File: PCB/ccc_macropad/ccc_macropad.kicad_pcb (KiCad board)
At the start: 2 copper layers, 101.5 x 44 mm, 18 parts, among them SW1 SW_Push, SW2 SW_Push, SW3 OS/Left_Right-hand_Switch, SW4 SW_Push, SW5 SW_Push, U1 RP2040-Zero

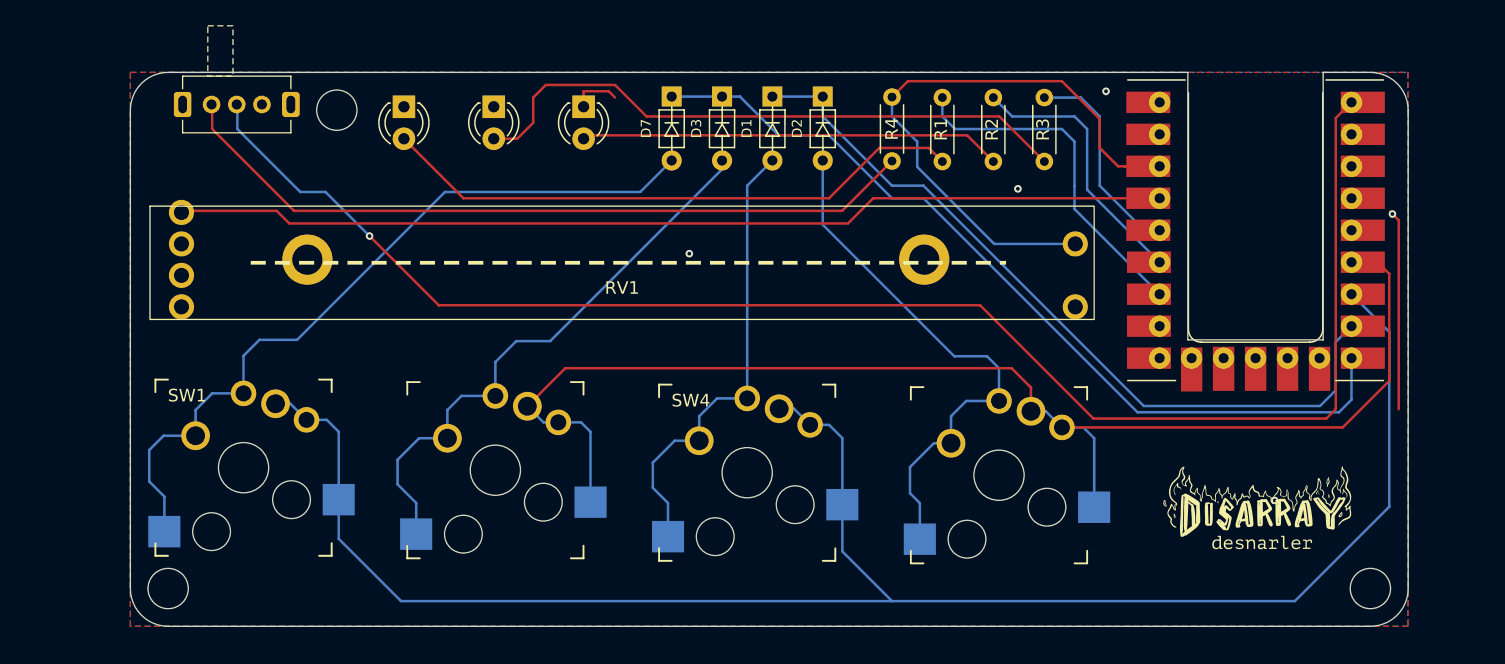
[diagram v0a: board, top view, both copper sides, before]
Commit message: feat: add buffer capacitor//increase board size// add foot holes
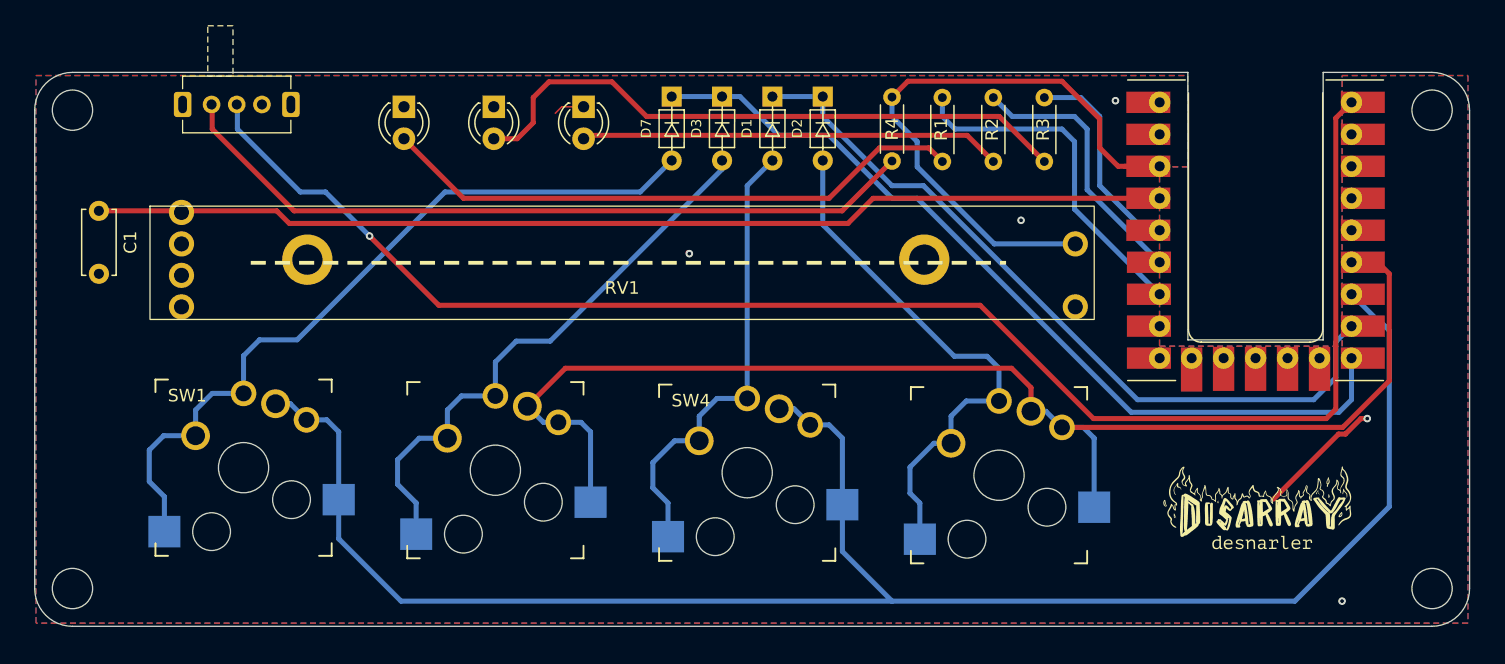
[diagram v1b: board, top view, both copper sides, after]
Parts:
- added C1: C, Capacitor_THT:C_Disc_D5.0mm_W2.5mm_P5.00mm, F.Cu at (108.0, 49.0)
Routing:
- net GND: track 20.4 -> 12.7 mm
- net Net-(U1-GP29): track 78.1 -> 84.7 mm
- net Net-(D1-K): track 62.0 -> 61.0 mm
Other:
- board size 101.5 x 44 mm -> 114 x 44 mm

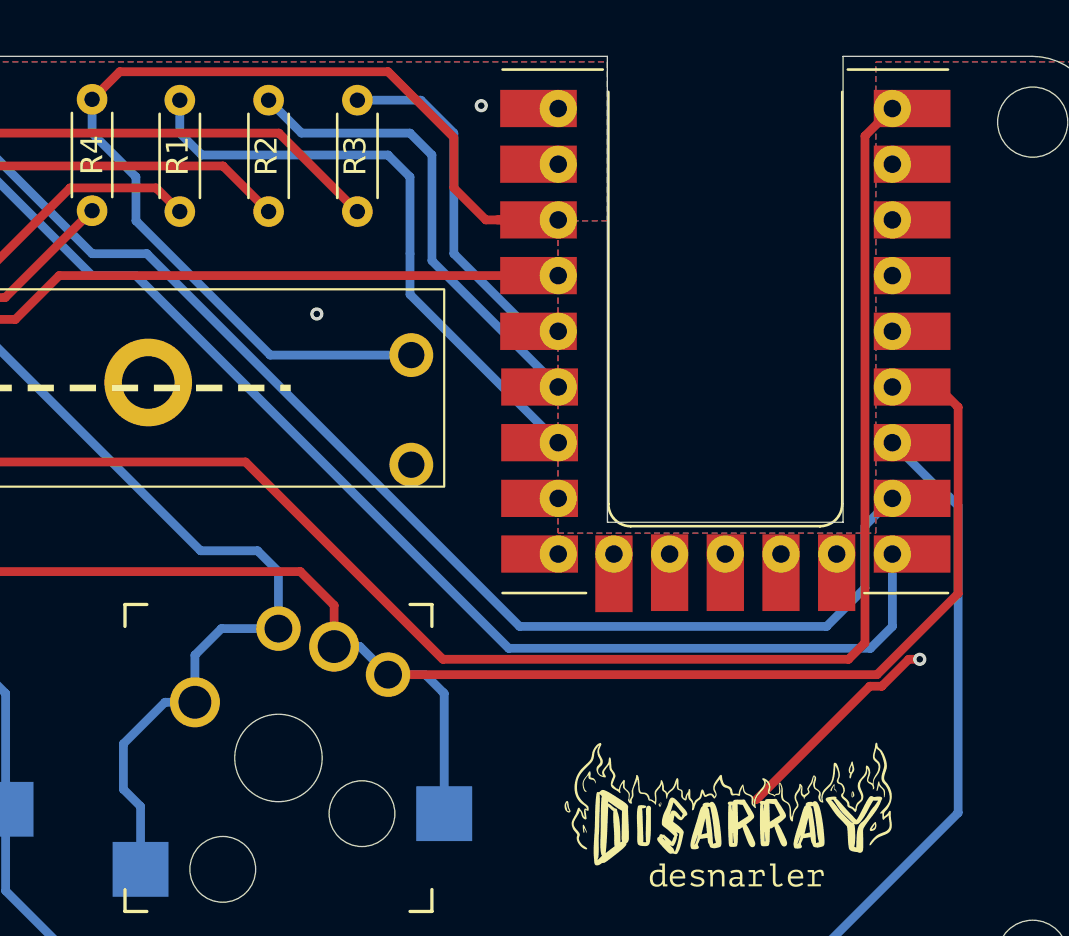
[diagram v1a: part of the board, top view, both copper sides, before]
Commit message: refactoring: mini adjustments
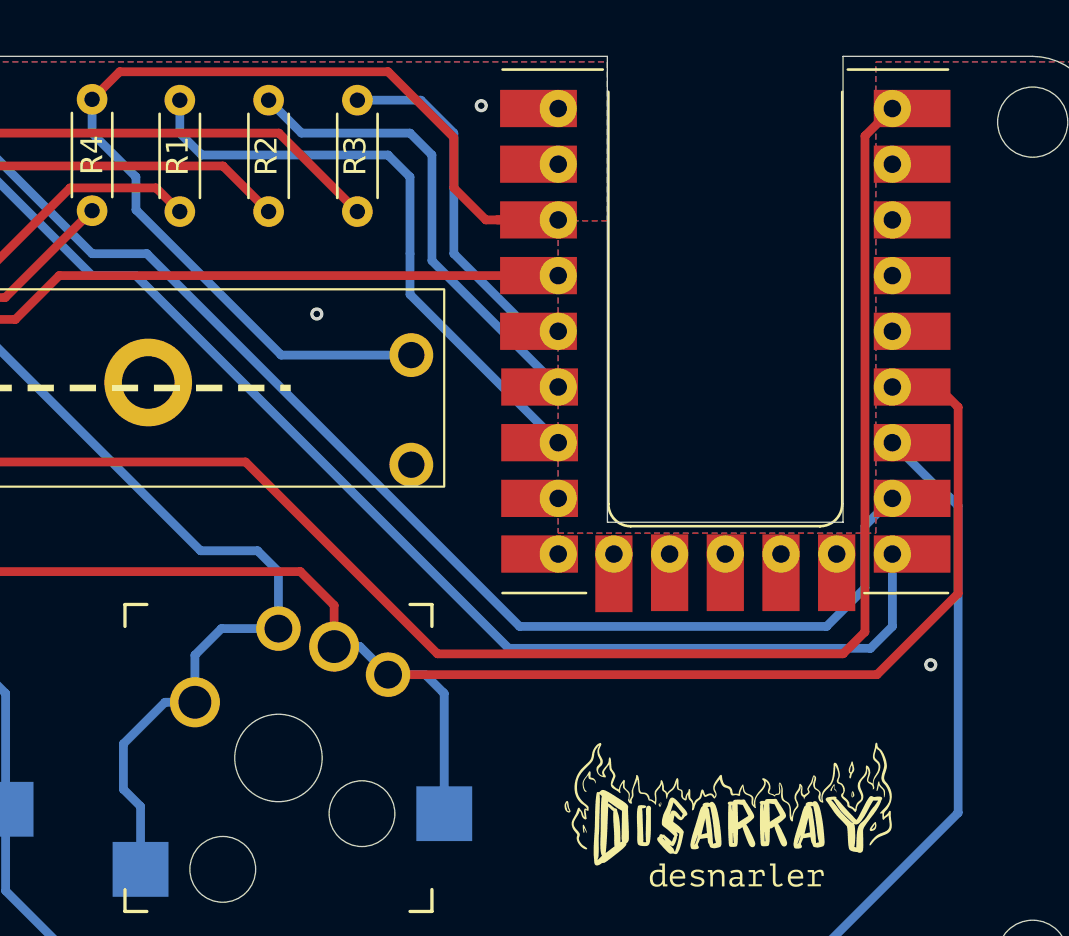
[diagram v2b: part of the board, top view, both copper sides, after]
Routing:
- net GND: track 12.7 -> 2.61 mm
- net Net-(SW3-B): track 124.0 -> 123.5 mm
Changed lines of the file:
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@@
-	)
-	(segment
-		(start 208.246704 65.5)
-		(end 208.75 65.5)
-		(width 0.4)
-		(layer "F.Cu")
-		(net 8)
-	)
-	(segment
-		(start 207.018704 66.728)
-		(end 208.246704 65.5)
-		(width 0.4)
-		(layer "F.Cu")
-		(net 8)
 	)
 	(segment
@@
 	)
 	(segment
-		(start 201.3 71.9)
-		(end 206.472 66.728)
-		(width 0.4)
-		(layer "F.Cu")
-		(net 8)
-	)
-	(segment
-		(start 206.472 66.728)
-		(end 207.018704 66.728)
-		(width 0.4)
-		(layer "F.Cu")
-		(net 8)
-	)
-	(segment
 		(start 154.8 52.3)
 		(end 154.9 52.4)
@@
 	)
 	(via
-		(at 208.75 65.5)
+		(at 209.25 65.75)
 		(size 0.6)
 		(drill 0.3)
@@
 	)
 	(segment
-		(start 187 65.5)
-		(end 205.5 65.5)
-		(width 0.4)
-		(layer "F.Cu")
-		(net 12)
-	)
-	(segment
-		(start 206.25 64.75)
+		(start 178 56.5)
+		(end 186.75 65.25)
+		(width 0.4)
+		(layer "F.Cu")
+		(net 12)
+	)
+	(segment
+		(start 205.25 65.25)
+		(end 206.25 64.25)
+		(width 0.4)
+		(layer "F.Cu")
+		(net 12)
+	)
+	(segment
+		(start 186.75 65.25)
+		(end 205.25 65.25)
+		(width 0.4)
+		(layer "F.Cu")
+		(net 12)
+	)
+	(segment
+		(start 206.25 41.63)
+		(end 207.5 40.38)
+		(width 0.4)
+		(layer "F.Cu")
+		(net 12)
+	)
+	(segment
+		(start 206.25 64.25)
 		(end 206.25 41.63)
 		(width 0.4)
@@
 		(net 12)
 	)
-	(segment
-		(start 206.25 41.63)
-		(end 207.5 40.38)
-		(width 0.4)
-		(layer "F.Cu")
-		(net 12)
-	)
-	(segment
-		(start 178 56.5)
-		(end 187 65.5)
-		(width 0.4)
-		(layer "F.Cu")
-		(net 12)
-	)
-	(segment
-		(start 205.5 65.5)
-		(end 206.25 64.75)
-		(width 0.4)
-		(layer "F.Cu")
-		(net 12)
-	)
 	(via
 		(at 129.5 51)
@@
 	)
 	(segment
-		(start 179.125 51.625)
-		(end 184.56 51.625)
-		(width 0.4)
-		(layer "B.Cu")
-		(net 16)
-	)
-	(segment
 		(start 171 39.96)
 		(end 171 41.5)
@@
 	)
 	(segment
-		(start 173 43.5)
-		(end 173 45.5)
-		(width 0.4)
-		(layer "B.Cu")
-		(net 16)
-	)
-	(segment
-		(start 173 45.5)
-		(end 179.125 51.625)
+		(start 173 45)
+		(end 179.625 51.625)
+		(width 0.4)
+		(layer "B.Cu")
+		(net 16)
+	)
+	(segment
+		(start 179.625 51.625)
+		(end 184.56 51.625)
 		(width 0.4)
 		(layer "B.Cu")
@@
 		(width 0.4)
 		(layer "B.Cu")
+		(net 16)
+	)
+	(segment
+		(start 173 43.5)
+		(end 173 45)
+		(width 0.4)
+		(layer "B.Cu")

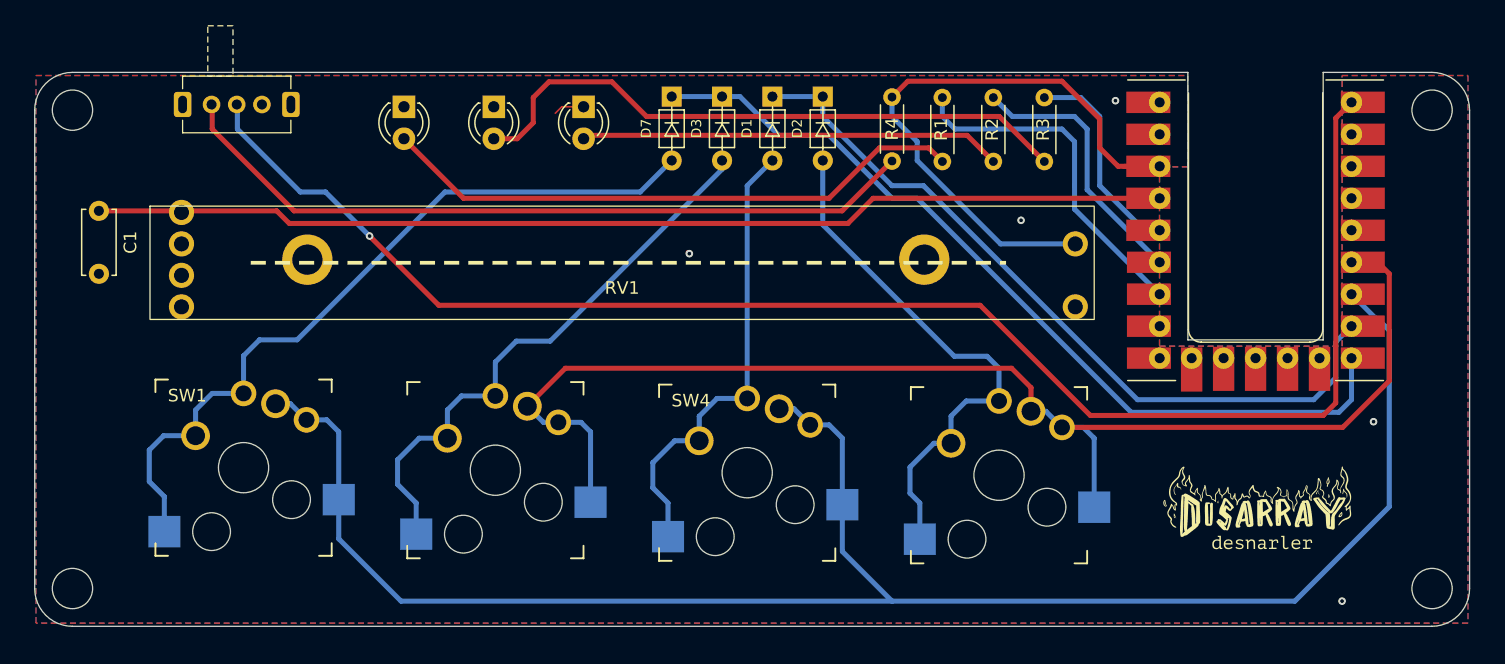
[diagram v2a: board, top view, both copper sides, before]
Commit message: new silkscreen design for the front of v1.1
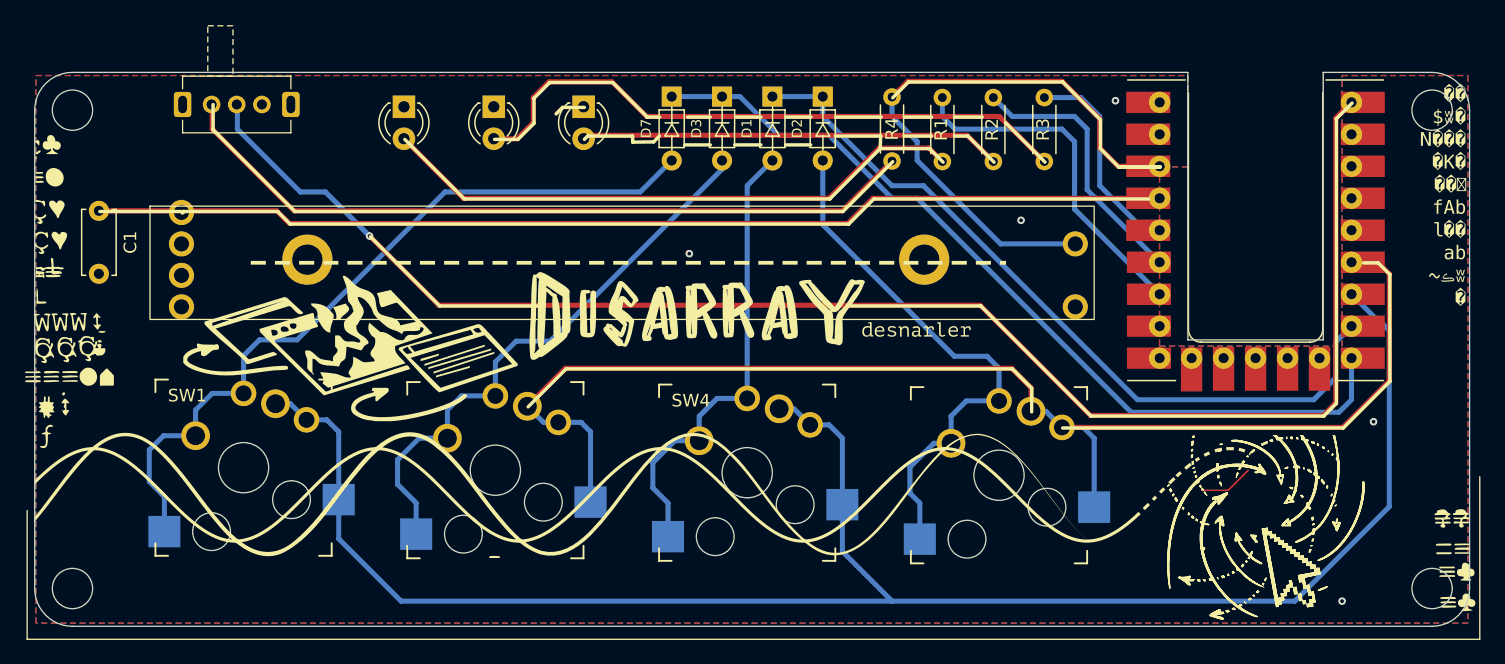
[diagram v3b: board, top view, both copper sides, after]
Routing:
- net (no net): track 0.00 -> 4.36 mm

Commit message: feat: create gerbers
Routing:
- net (no net): track 4.36 -> 0.00 mm
